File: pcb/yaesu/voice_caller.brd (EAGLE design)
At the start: 52.4 x 63.1 mm, 56 parts, among them IC1 78L12SMD, IC2 LM386M-1, IC3 25F32006WSOI

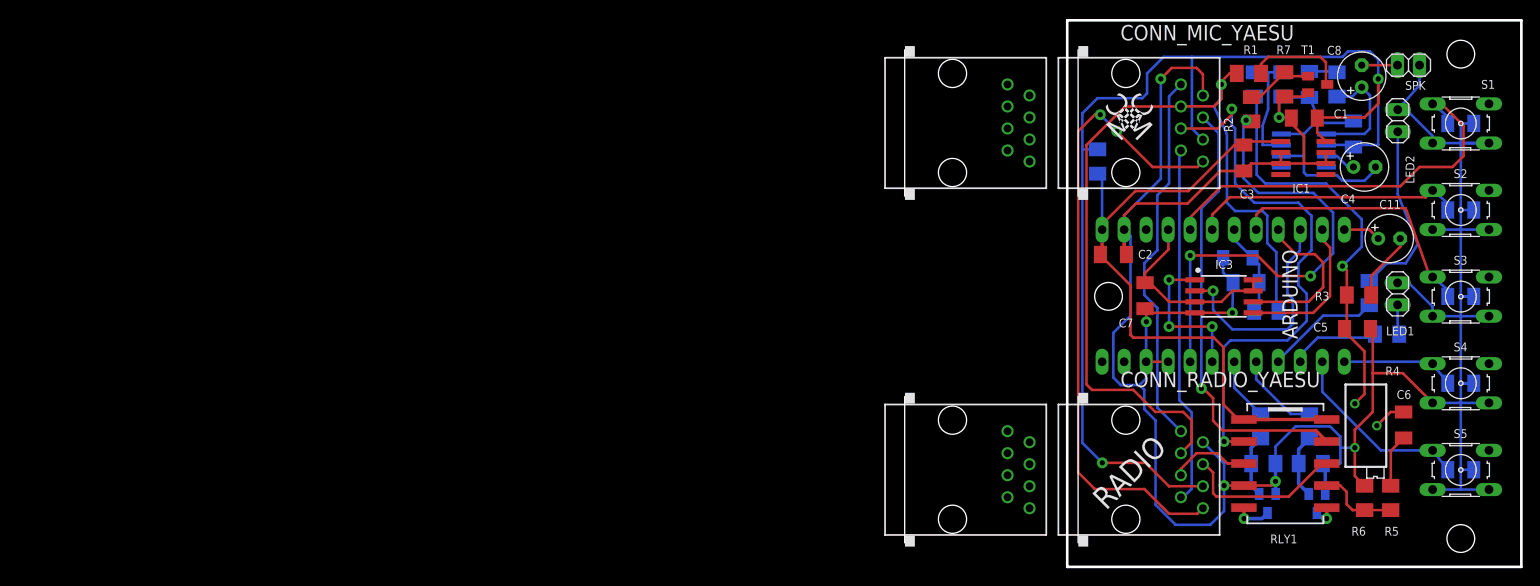
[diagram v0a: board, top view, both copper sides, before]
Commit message: Connector connections corredted.
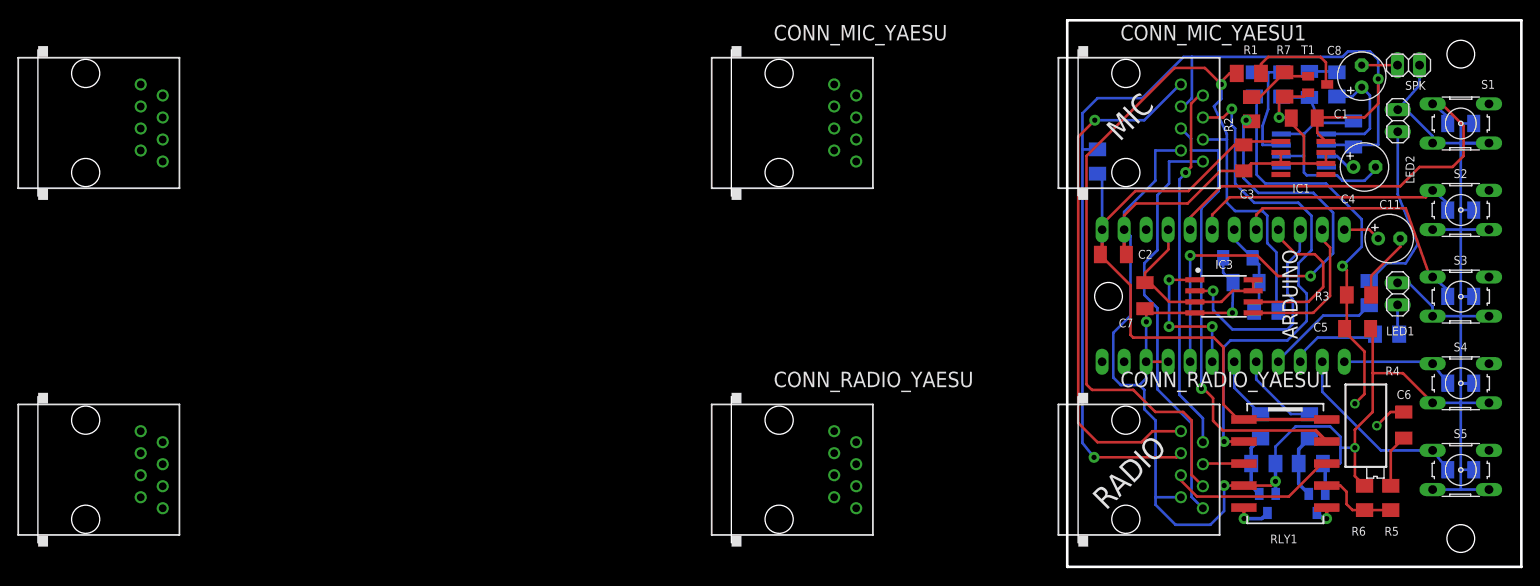
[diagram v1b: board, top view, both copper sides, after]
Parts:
- added CONN_MIC_YAESU1, CONN_RADIO_YAESU1: RJ45-8L-B, con-tycoelectronics:RJ45-NO-SHIELD
- moved CONN_MIC_ICOM 100.0 mm to (-118.0, 20.0)
- moved CONN_RADIO_ICOM 100.0 mm to (-118.0, -20.0)
- moved CONN_MIC_YAESU 40.0 mm to (-38.0, 20.0)
- moved CONN_RADIO_YAESU 40.0 mm to (-38.0, -20.0)
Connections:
- net +8V: now also CONN_MIC_YAESU1.3, CONN_RADIO_YAESU1.3
- net AF_OUT: now also CONN_MIC_YAESU1.1, CONN_RADIO_YAESU1.1
- net FREQ_UD: now also CONN_MIC_YAESU1.8, CONN_RADIO_YAESU1.8
- net GND: now also CONN_MIC_YAESU1.7, CONN_RADIO_YAESU1.7
- net MIC: now also CONN_MIC_YAESU1.5
- net MIC_GND: now also CONN_MIC_YAESU1.4
- net MIC_GND_RADIO: now also CONN_RADIO_YAESU1.4
- net MIC_RADIO: now also CONN_RADIO_YAESU1.5
- net PTT: now also CONN_MIC_YAESU1.6, CONN_RADIO_YAESU1.6
- net SQUELCH: now also CONN_MIC_YAESU1.2, CONN_RADIO_YAESU1.2
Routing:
- net GND: track 358.3 -> 341.5 mm, vias 6 -> 5
- net AF_OUT: track 73.9 -> 60.7 mm, vias 2 -> 1
- net +8V: track 134.6 -> 126.0 mm
- net PTT: track 99.3 -> 105.7 mm
- net MIC_GND_RADIO: track 9.24 -> 4.76 mm
- net FREQ_UD: track 43.5 -> 47.9 mm
- net MIC_GND: track 63.9 -> 60.0 mm
- net MIC: track 51.4 -> 53.0 mm
- net SQUELCH: track 41.3 -> 42.5 mm, vias 0 -> 1
- net MIC_RADIO: track 18.8 -> 19.8 mm
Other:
- board text added: "FT-817 FT-857"
